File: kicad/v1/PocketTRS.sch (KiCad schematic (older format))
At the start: 33 parts, among them J1 TRS-80, J2 AudioJack3, J3 Mini-DIN-6, J4 DB15_Female_HighDensity, J5 Programmer, J6 USB_B_Micro, J7 PTRS_RESET, J8 ESP_RESET, Q1 2N7000, SW1 SW_Push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

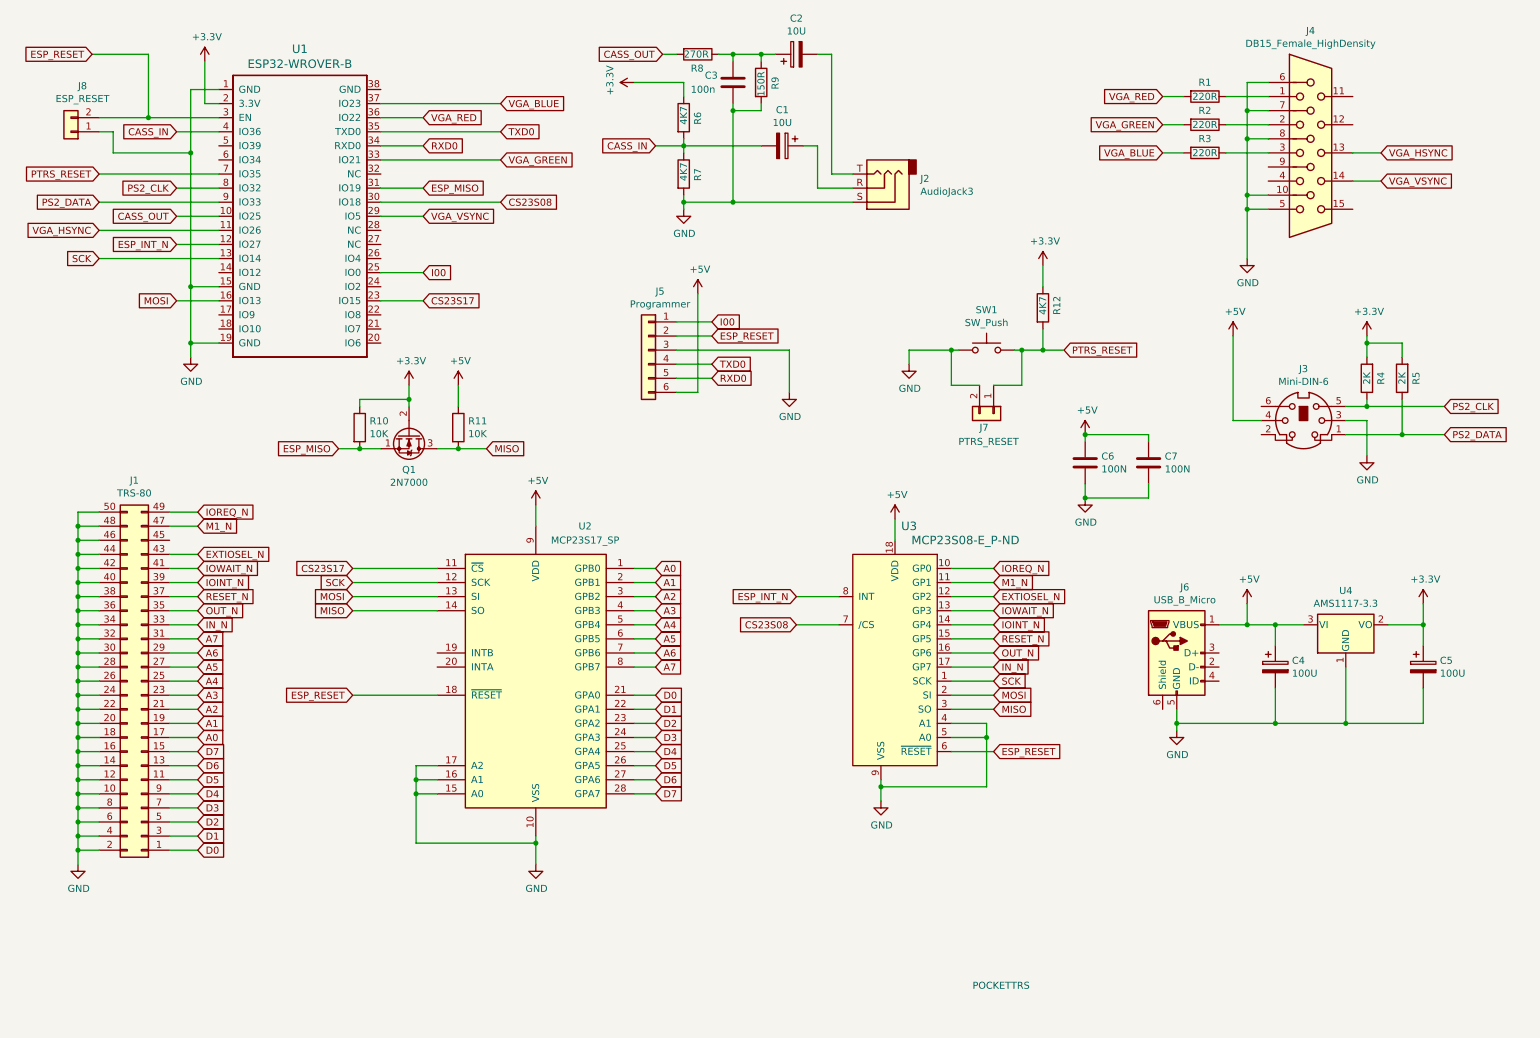
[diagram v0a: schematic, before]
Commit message: Added MCP43x1 quadpot for screen color
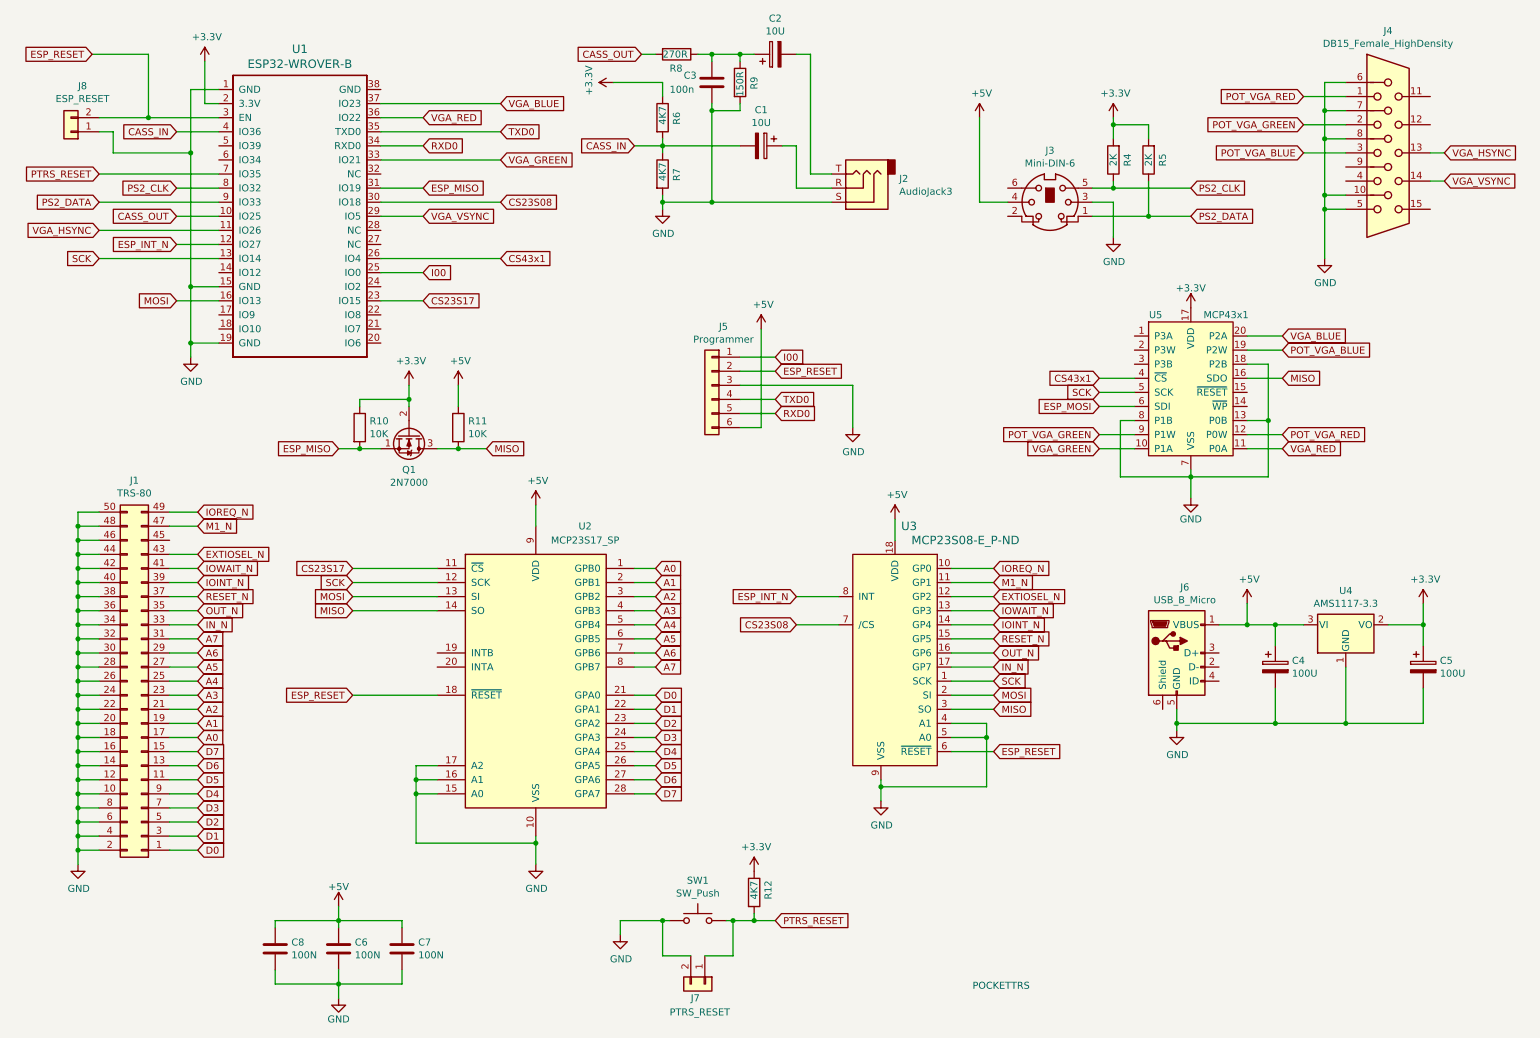
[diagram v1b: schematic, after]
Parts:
- removed R1, R2, R3: 220R, Resistors_THT:R_Axial_DIN0207_L6.3mm_D2.5mm_P7.62mm_Horizontal, symbol Device:R
- added C8: 100N, Capacitors_THT:C_Disc_D3.0mm_W2.0mm_P2.50mm, symbol Device:C
- added U5: MCP43x1, symbol MCP43X1:MCP43x1
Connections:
- net +3V3: now also U5.17 (VDD)
- net +5V: now also C8.1
- net GND: now also C8.2, U5.13 (P0B), U5.18 (P2B), U5.7 (VSS), U5.8 (P1B)
- net MISO: now also U5.16 (SDO)
- net SCK: now also U5.5 (SCK)
- net VGA_BLUE: now also U5.20 (P2A)
- net VGA_GREEN: now also U5.10 (P1A)
- net VGA_RED: now also U5.11 (P0A)
- net POT_VGA_RED: now reaches J4.1
- net POT_VGA_RED: now also U5.12 (P0W)
- net POT_VGA_GREEN: now reaches J4.2
- net POT_VGA_GREEN: now also U5.9 (P1W)
- net POT_VGA_BLUE: now reaches J4.3
- net POT_VGA_BLUE: now also U5.19 (P2W)
- net CS43x1: now reaches U1.26 (IO4)
- net CS43x1: now also U5.4 (~CS)
- new net ESP_MOSI: U5.6 (SDI)
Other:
- moved on the sheet: C1, C2, C3, C6, C7, J2, J3, J4, J5, J7, R12, R4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

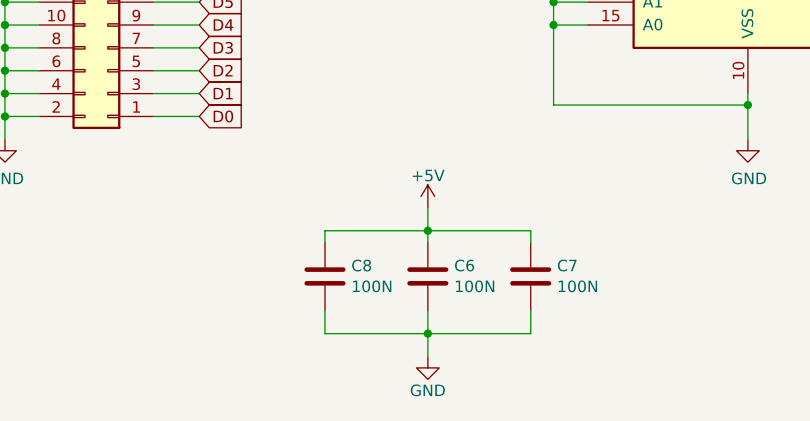
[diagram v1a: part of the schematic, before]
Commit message: C8/C9 to 3.3V
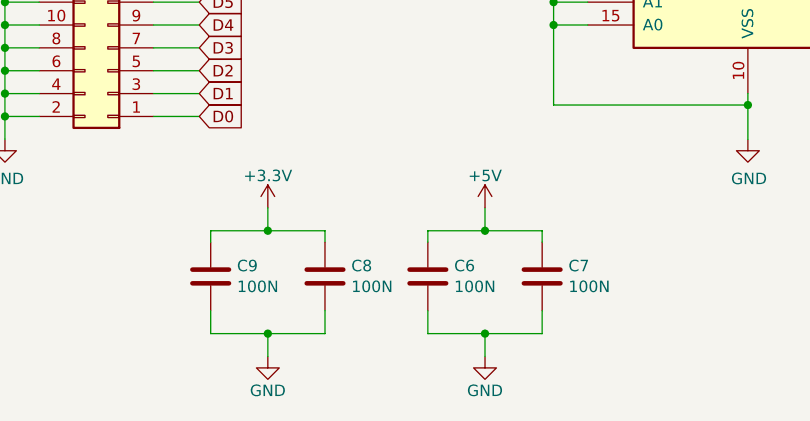
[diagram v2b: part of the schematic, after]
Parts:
- added C9: 100N, Capacitors_THT:C_Disc_D3.0mm_W2.0mm_P2.50mm, symbol Device:C
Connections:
- net +3V3: now also C8.1, C9.1
- net +5V: no longer C8.1
- net GND: now also C9.2
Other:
- moved on the sheet: C7
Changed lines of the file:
@@
 L Device:C C7
 U 1 1 5EC77E32
-P 3300 7200
-F 0 "C7" H 3415 7246 50  0000 L CNN
-F 1 "100N" H 3415 7155 50  0000 L CNN
-F 2 "Capacitors_THT:C_Disc_D3.0mm_W2.0mm_P2.50mm" H 3338 7050 50  0001 C CNN
-F 3 "~" H 3300 7200 50  0001 C CNN
-	1    3300 7200
+P 3350 7200
+F 0 "C7" H 3465 7246 50  0000 L CNN
+F 1 "100N" H 3465 7155 50  0000 L CNN
+F 2 "Capacitors_THT:C_Disc_D3.0mm_W2.0mm_P2.50mm" H 3388 7050 50  0001 C CNN
+F 3 "~" H 3350 7200 50  0001 C CNN
+	1    3350 7200
 	1    0    0    -1
 $EndComp
 Wire Wire Line
 	2850 7050 2850 7000
-Wire Wire Line
-	2850 7000 3300 7000
-Wire Wire Line
-	3300 7000 3300 7050
-Wire Wire Line
-	2850 7350 2850 7450
-Wire Wire Line
-	2850 7450 3300 7450
-Wire Wire Line
-	3300 7450 3300 7350
 Wire Wire Line
 	3150 1300 3450 1300
@@
 	1    0    0    -1
 $EndComp
-Wire Wire Line
-	2400 7050 2400 7000
-Wire Wire Line
-	2400 7350 2400 7450
-Connection ~ 2850 7450
-Connection ~ 2850 7000
 $Comp
 L power:GND #PWR0123
 U 1 1 5F246F51
-P 2850 7550
-F 0 "#PWR0123" H 2850 7300 50  0001 C CNN
-F 1 "GND" H 2850 7400 50  0000 C CNN
-F 2 "" H 2850 7550 50  0001 C CNN
-F 3 "" H 2850 7550 50  0001 C CNN
-	1    2850 7550
+P 3100 7550
+F 0 "#PWR0123" H 3100 7300 50  0001 C CNN
+F 1 "GND" H 3100 7400 50  0000 C CNN
+F 2 "" H 3100 7550 50  0001 C CNN
+F 3 "" H 3100 7550 50  0001 C CNN
+	1    3100 7550
 	1    0    0    -1
 $EndComp
@@
 L power:+5V #PWR0124
 U 1 1 5F247655
-P 2850 6900
-F 0 "#PWR0124" H 2850 6750 50  0001 C CNN
-F 1 "+5V" H 2850 7040 50  0000 C CNN
-F 2 "" H 2850 6900 50  0001 C CNN
-F 3 "" H 2850 6900 50  0001 C CNN
-	1    2850 6900
+P 3100 6900
+F 0 "#PWR0124" H 3100 6750 50  0001 C CNN
+F 1 "+5V" H 3100 7040 50  0000 C CNN
+F 2 "" H 3100 6900 50  0001 C CNN
+F 3 "" H 3100 6900 50  0001 C CNN
+	1    3100 6900
 	1    0    0    -1
 $EndComp
@@
 	8900 3850 8900 4000
 Wire Wire Line
-	2400 7450 2850 7450
-Wire Wire Line
-	2400 7000 2850 7000
-Wire Wire Line
-	2850 6900 2850 7000
-Wire Wire Line
-	2850 7550 2850 7450
-Wire Wire Line
 	9300 3450 9450 3450
 Connection ~ 9450 3450
@@
 	8400 3850 8900 3850
 $Comp
-L power:+3.3V #PWR?
+L power:+3.3V #PWR0116
 U 1 1 5EEB1E42
 P 8900 2650
-F 0 "#PWR?" H 8900 2500 50  0001 C CNN
+F 0 "#PWR0116" H 8900 2500 50  0001 C CNN
 F 1 "+3.3V" H 8900 2790 50  0000 C CNN
 F 2 "" H 8900 2650 50  0001 C CNN
@@
 	1    0    0    -1
 $EndComp
+$Comp
+L Device:C C9
+U 1 1 5EF05C1D
+P 1900 7200
+F 0 "C9" H 2015 7246 50  0000 L CNN
+F 1 "100N" H 2015 7155 50  0000 L CNN
+F 2 "Capacitors_THT:C_Disc_D3.0mm_W2.0mm_P2.50mm" H 1938 7050 50  0001 C CNN
+F 3 "~" H 1900 7200 50  0001 C CNN
+	1    1900 7200
+	1    0    0    -1
+$EndComp
+$Comp
+L power:+3.3V #PWR0127
+U 1 1 5EF56273
+P 2150 6900
+F 0 "#PWR0127" H 2150 6750 50  0001 C CNN
+F 1 "+3.3V" H 2150 7040 50  0000 C CNN
+F 2 "" H 2150 6900 50  0001 C CNN
+F 3 "" H 2150 6900 50  0001 C CNN
+	1    2150 6900
+	1    0    0    -1
+$EndComp
+Wire Wire Line
+	2850 7000 3100 7000
+Wire Wire Line
+	3350 7000 3350 7050
+Wire Wire Line
+	3350 7350 3350 7450
+Wire Wire Line
+	3350 7450 3100 7450
+Wire Wire Line
+	2850 7450 2850 7350
+Wire Wire Line
+	2400 7350 2400 7450
+Wire Wire Line
+	2400 7450 2150 7450
+Wire Wire Line
+	1900 7450 1900 7350
+Wire Wire Line
+	2400 7050 2400 7000
+Wire Wire Line
+	2400 7000 2150 7000
+Wire Wire Line
+	1900 7000 1900 7050
+Wire Wire Line
+	2150 6900 2150 7000
+Connection ~ 2150 7000
+Wire Wire Line
+	2150 7000 1900 7000
+Wire Wire Line
+	3100 6900 3100 7000
+Connection ~ 3100 7000
+Wire Wire Line
+	3100 7000 3350 7000
+$Comp
+L power:GND #PWR?
+U 1 1 5F078B92
+P 2150 7550
+F 0 "#PWR?" H 2150 7300 50  0001 C CNN
+F 1 "GND" H 2150 7400 50  0000 C CNN
+F 2 "" H 2150 7550 50  0001 C CNN
+F 3 "" H 2150 7550 50  0001 C CNN
+	1    2150 7550
+	1    0    0    -1
+$EndComp
+Wire Wire Line
+	2150 7550 2150 7450
+Connection ~ 2150 7450
+Wire Wire Line
+	2150 7450 1900 7450
+Wire Wire Line
+	3100 7550 3100 7450
+Connection ~ 3100 7450
+Wire Wire Line
+	3100 7450 2850 7450
 $EndSCHEMATC
